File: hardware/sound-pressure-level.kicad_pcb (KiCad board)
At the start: 2 copper layers, 25 x 25 mm, 26 parts, among them P1 CON-SENSOR2, P2 BOOT, U1 XMC1XXX48, U2 DRILL, U3 DRILL, U4 DRILL, U5 DRILL, U6 ICS-43432, X1 16MHz

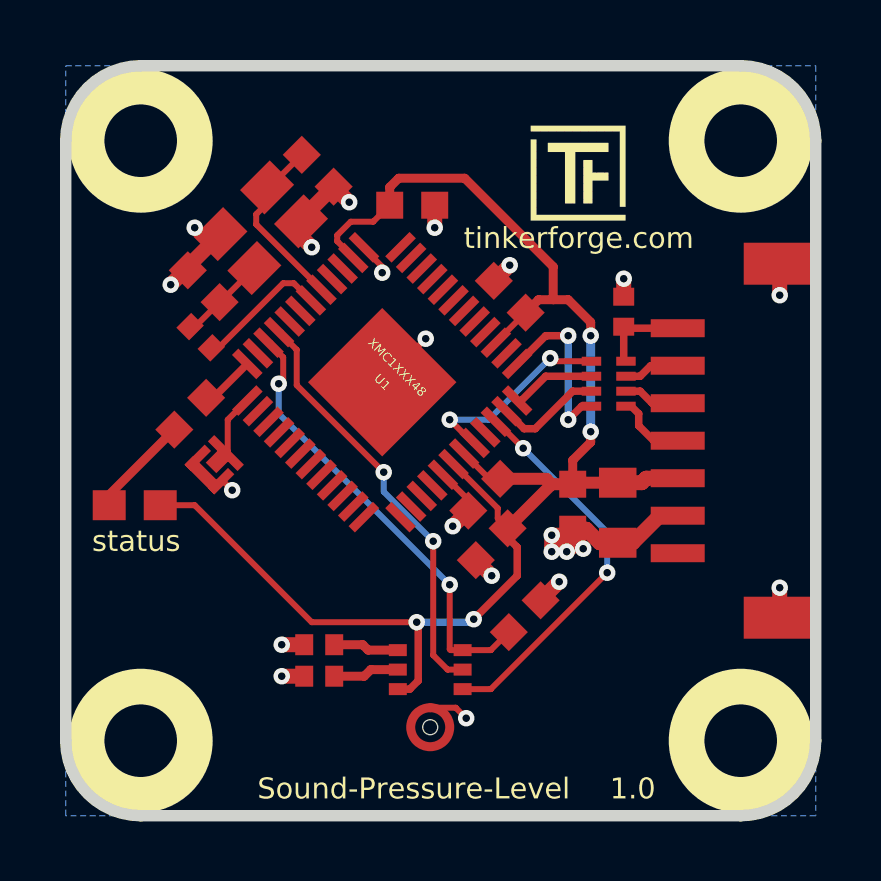
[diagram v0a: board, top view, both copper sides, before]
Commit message: Add capacitor for microphone & logos
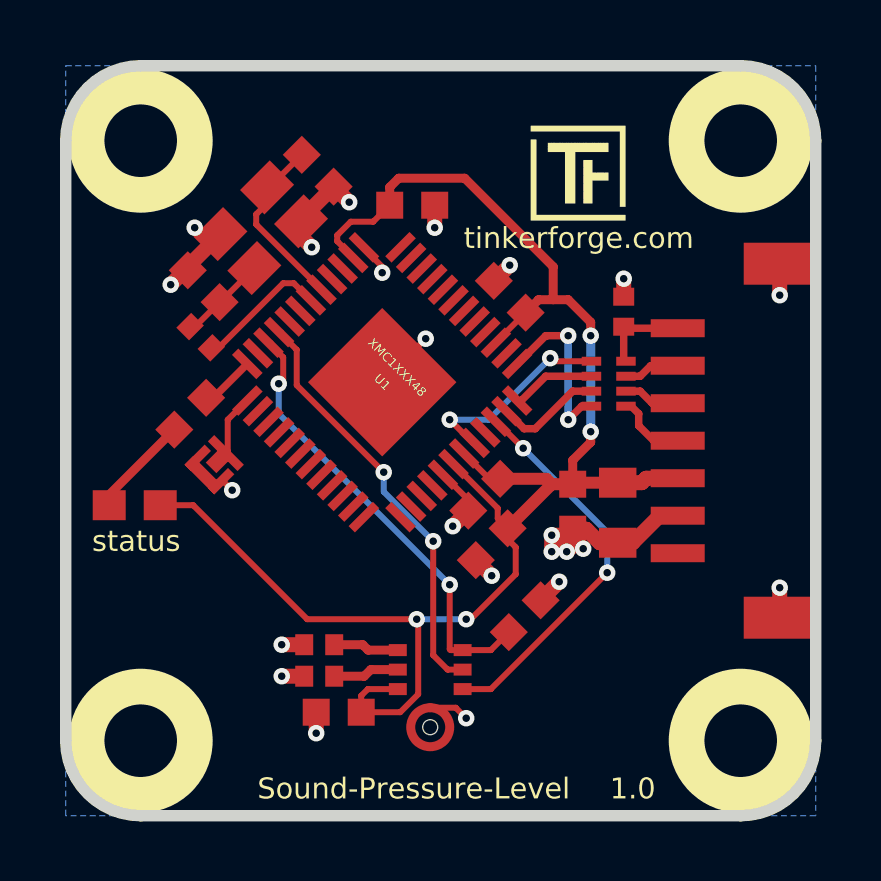
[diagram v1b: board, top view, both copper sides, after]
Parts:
- added C10: 100nF, kicad-libraries:C0603F, F.Cu at (139.2, 150.1)
- added G***: LOGO, kicad-libraries:Logo_CoMCU, B.Cu at (147.1, 132.2)
- added VAL: WEEE_7mm, kicad-libraries:WEEE_7mm, B.Cu at (133.9, 141.0)
- added VAL: CE_5mm, kicad-libraries:CE_5mm, B.Cu at (150.1, 141.0)
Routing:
- net VCC: track 52.6 -> 56.5 mm
- net GND: track 29.8 -> 32.4 mm, vias 22 -> 23

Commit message: add fiducial marks
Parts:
- added Fiducial_Mark: VAL**, kicad-libraries:Fiducial_Mark, F.Cu at (131.6, 135.0)
- added Fiducial_Mark: VAL**, kicad-libraries:Fiducial_Mark, F.Cu at (153.6, 144.5)
- added Fiducial_Mark: VAL**, kicad-libraries:Fiducial_Mark, F.Cu at (134.6, 147.5)
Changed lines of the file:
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@@
-(kicad_pcb (version 4) (host pcbnew 4.0.2+dfsg1-stable)
+(kicad_pcb (version 4) (host pcbnew 4.0.7-e2-6376~58~ubuntu17.04.1)
   (general
     (links 61)
     (no_connects 0)
-    (area 129.909499 128.309499 155.290501 153.690501)
+    (area 129.244999 127.644999 275.49286 158.115)
     (thickness 1.6)
     (drawings 13)
     (tracks 249)
     (zones 0)
-    (modules 30)
+    (modules 33)
     (nets 54)
   )
@@
       (xy 1.301301 2.715081) (xy 1.302426 2.714986)) (layer B.SilkS) (width 0.01))
   )
+  (module kicad-libraries:Fiducial_Mark (layer F.Cu)
+    (at 131.6 135)
+    (attr smd)
+    (fp_text reference Fiducial_Mark (at 0 0) (layer F.SilkS) hide
+      (effects (font (size 0.127 0.127) (thickness 0.03302)))
+    )
+    (fp_text value VAL** (at 0 -0.29972) (layer F.SilkS) hide
+      (effects (font (size 0.127 0.127) (thickness 0.03302)))
+    )
+    (fp_circle (center 0 0) (end 1.15062 0) (layer Dwgs.User) (width 0.01016))
+    (pad 1 smd circle (at 0 0) (size 1.00076 1.00076) (layers F.Cu F.Paste F.Mask)
+      (clearance 0.65024))
+  )
+  (module kicad-libraries:Fiducial_Mark (layer F.Cu)
+    (at 153.6 144.5)
+    (attr smd)
+    (fp_text reference Fiducial_Mark (at 0 0) (layer F.SilkS) hide
+      (effects (font (size 0.127 0.127) (thickness 0.03302)))
+    )
+    (fp_text value VAL** (at 0 -0.29972) (layer F.SilkS) hide
+      (effects (font (size 0.127 0.127) (thickness 0.03302)))
+    )
+    (fp_circle (center 0 0) (end 1.15062 0) (layer Dwgs.User) (width 0.01016))
+    (pad 1 smd circle (at 0 0) (size 1.00076 1.00076) (layers F.Cu F.Paste F.Mask)
+      (clearance 0.65024))
+  )
+  (module kicad-libraries:Fiducial_Mark (layer F.Cu)
+    (at 134.6 147.5)
+    (attr smd)
+    (fp_text reference Fiducial_Mark (at 0 0) (layer F.SilkS) hide
+      (effects (font (size 0.127 0.127) (thickness 0.03302)))
+    )
+    (fp_text value VAL** (at 0 -0.29972) (layer F.SilkS) hide
+      (effects (font (size 0.127 0.127) (thickness 0.03302)))
+    )
+    (fp_circle (center 0 0) (end 1.15062 0) (layer Dwgs.User) (width 0.01016))
+    (pad 1 smd circle (at 0 0) (size 1.00076 1.00076) (layers F.Cu F.Paste F.Mask)
+      (clearance 0.65024))
+  )
   (gr_line (start 152.6 128.5) (end 132.6 128.5) (angle 90) (layer Edge.Cuts) (width 0.381))

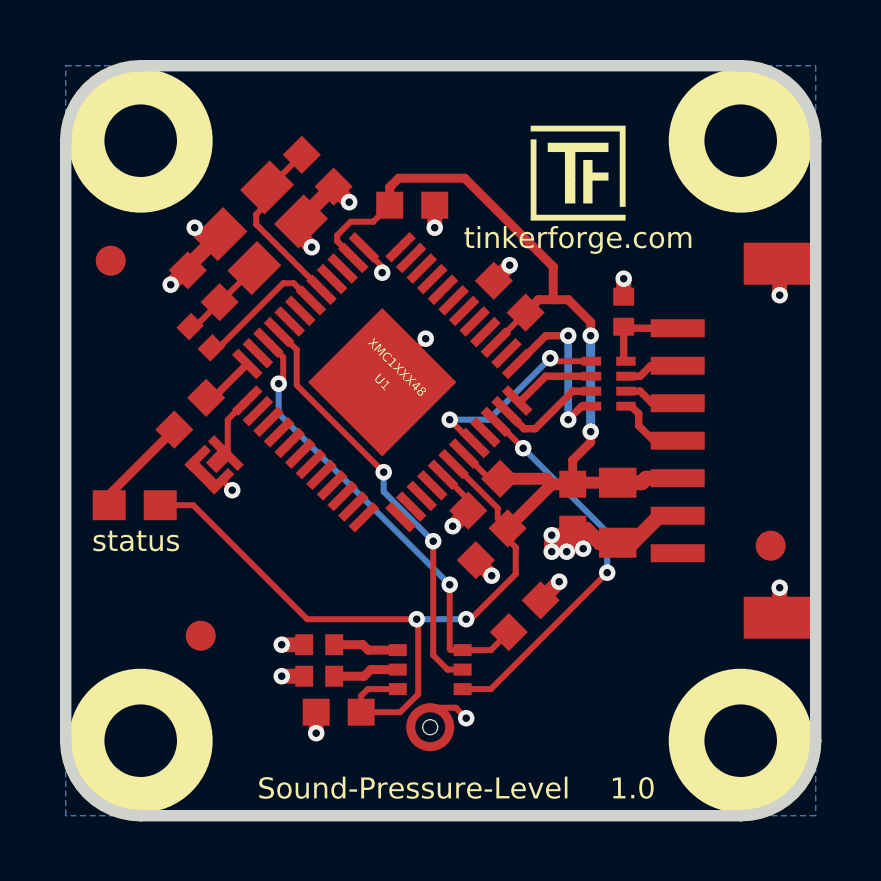
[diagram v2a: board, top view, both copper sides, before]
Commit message: Remove R9
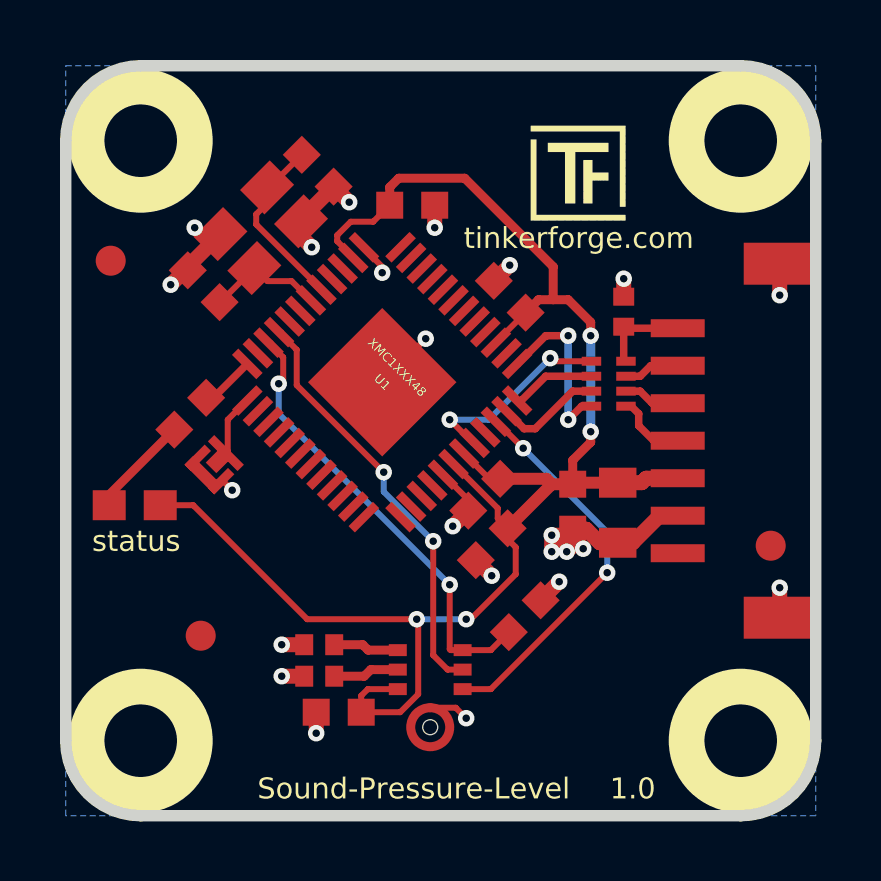
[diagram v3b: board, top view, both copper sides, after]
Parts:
- removed R9: TBD, kicad-libraries:R0402F
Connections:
- U1 pad 42: Net-(R9-Pad1) -> Net-(C9-Pad1)
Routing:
- net Net-(R9-Pad1): track 4.45 -> 0.00 mm
- net Net-(C9-Pad1): track 2.95 -> 3.96 mm

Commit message: Add debug pad
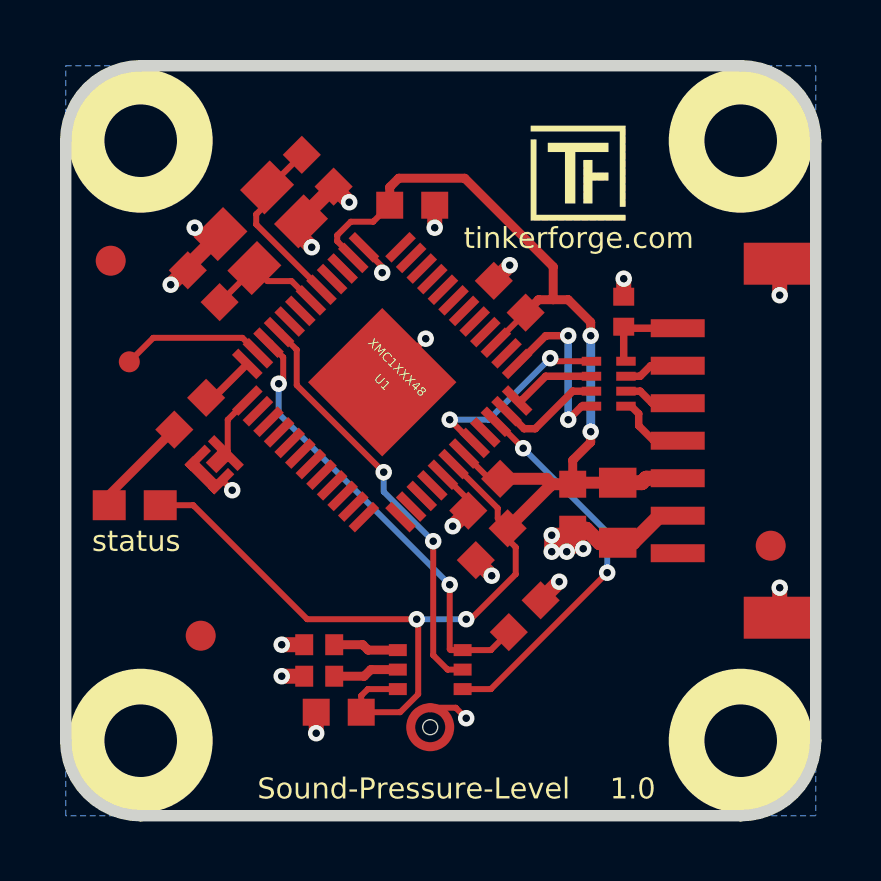
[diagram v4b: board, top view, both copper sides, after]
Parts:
- added P3: DEBUG, kicad-libraries:DEBUG_PAD, F.Cu at (132.2, 138.4)
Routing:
- net Net-(P3-Pad1): track 0.00 -> 4.83 mm
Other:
- board text added: "Copyright Tinkerforge GmbH 2018. This documentation describes Open Hardware and is licensed under the CERN OHL v. 1.1. You may redistribute and modify this documentation under the terms of the CERN OHL v.1.1. (http://ohwr.org/cernohl). This documentation is distributed WITHOUT ANY EXPRESS OR IMPLIED WARRANTY, INCLUDING OF MERCHANTABILITY, SATISFACTORY QUALITY AND FITNESS FOR A PARTICULAR PURPOSE.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"
- board text removed: "Copyright Tinkerforge GmbH 2017. This documentation describes Open Hardware and is licensed under the CERN OHL v. 1.1. You may redistribute and modify this documentation under the terms of the CERN OHL v.1.1. (http://ohwr.org/cernohl). This documentation is distributed WITHOUT ANY EXPRESS OR IMPLIED WARRANTY, INCLUDING OF MERCHANTABILITY, SATISFACTORY QUALITY AND FITNESS FOR A PARTICULAR PURPOSE.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"
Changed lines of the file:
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@@
 (kicad_pcb (version 4) (host pcbnew 4.0.2+dfsg1-stable)
   (general
-    (links 60)
+    (links 61)
     (no_connects 0)
     (area 129.909499 128.309499 155.290501 153.690501)
     (thickness 1.6)
     (drawings 13)
-    (tracks 247)
+    (tracks 251)
     (zones 0)
-    (modules 32)
+    (modules 33)
     (nets 53)
   )
@@
   (title_block
     (title "Sound-Level-Pressure Bricklet")
-    (date 2017-11-30)
+    (date 2018-01-22)
     (rev 1.0)
     (company "Tinkerforge GmbH")
     (comment 1 "Licensed under CERN OHL v.1.1")
-    (comment 2 "Copyright (©) 2017, L.Lauer <lukas@tinkerforge.com>")
+    (comment 2 "Copyright (©) 2018, L.Lauer <lukas@tinkerforge.com>")
   )
   (layers
@@
   (net 48 "Net-(U1-Pad44)")
   (net 49 SCK)
-  (net 50 "Net-(U1-Pad47)")
-  (net 51 "Net-(R3-Pad1)")
-  (net 52 "Net-(R4-Pad1)")
+  (net 50 "Net-(R3-Pad1)")
+  (net 51 "Net-(R4-Pad1)")
+  (net 52 "Net-(P3-Pad1)")
   (net_class Default "This is the default net class."
     (clearance 0.15)
@@
     (add_net "Net-(P1-Pad6)")
     (add_net "Net-(P2-Pad2)")
+    (add_net "Net-(P3-Pad1)")
     (add_net "Net-(R1-Pad1)")
     (add_net "Net-(R3-Pad1)")
@@
     (add_net "Net-(U1-Pad43)")
     (add_net "Net-(U1-Pad44)")
-    (add_net "Net-(U1-Pad47)")
     (add_net "Net-(U1-Pad5)")
     (add_net "Net-(U1-Pad6)")
@@
       (net 17 SD))
     (pad 47 smd rect (at -3.61188 2.2479 45) (size 0.29972 1.14808) (layers F.Cu F.Paste F.Mask)
-      (net 50 "Net-(U1-Pad47)"))
+      (net 52 "Net-(P3-Pad1)"))
     (pad 48 smd rect (at -3.61188 2.74828 45) (size 0.29972 1.14808) (layers F.Cu F.Paste F.Mask)
       (net 16 "Net-(R1-Pad1)"))
@@
       (net 2 VCC))
     (pad 1 smd rect (at -2.57 1.08 270) (size 0.4 0.6) (layers F.Cu F.Paste F.Mask)
-      (net 51 "Net-(R3-Pad1)"))
+      (net 50 "Net-(R3-Pad1)"))
     (pad 2 smd rect (at -1.92 1.08 270) (size 0.4 0.6) (layers F.Cu F.Paste F.Mask)
-      (net 52 "Net-(R4-Pad1)"))
+      (net 51 "Net-(R4-Pad1)"))
   )
   (module kicad-libraries:CRYSTAL_3225 (layer F.Cu)
@@
       (net 1 GND))
     (pad 1 smd rect (at -0.5 0 180) (size 0.6 0.7) (layers F.Cu F.Paste F.Mask)
-      (net 51 "Net-(R3-Pad1)"))
+      (net 50 "Net-(R3-Pad1)"))
     (model Resistors_SMD/R_0402.wrl
       (at (xyz 0 0 0))
@@
       (net 1 GND))
     (pad 1 smd rect (at -0.5 0 180) (size 0.6 0.7) (layers F.Cu F.Paste F.Mask)
-      (net 52 "Net-(R4-Pad1)"))
+      (net 51 "Net-(R4-Pad1)"))
     (model Resistors_SMD/R_0402.wrl
       (at (xyz 0 0 0))
@@
       (clearance 0.65024))
   )
+  (module kicad-libraries:DEBUG_PAD (layer F.Cu)
+    (at 132.22 138.37)
+    (fp_text reference P3 (at 0 0.175) (layer F.Fab)
+      (effects (font (size 0.15 0.15) (thickness 0.0375)))
+    )
+    (fp_text value DEBUG (at 0 -0.15) (layer F.Fab)
+      (effects (font (size 0.15 0.15) (thickness 0.0375)))
+    )
+    (pad 1 smd circle (at 0 0) (size 0.7 0.7) (layers F.Cu F.Paste F.Mask)
+      (net 52 "Net-(P3-Pad1)"))
+  )
   (gr_line (start 152.6 128.5) (end 132.6 128.5) (angle 90) (layer Edge.Cuts) (width 0.381))
   (gr_line (start 132.6 153.5) (end 152.6 153.5) (angle 90) (layer Edge.Cuts) (width 0.381))
-  (gr_text "Copyright Tinkerforge GmbH 2017.\nThis documentation describes Open Hardware and is licensed under the\nCERN OHL v. 1.1.\nYou may redistribute and modify this documentation under the terms of the\nCERN OHL v.1.1. (http://ohwr.org/cernohl). This documentation is distributed\nWITHOUT ANY EXPRESS OR IMPLIED WARRANTY, INCLUDING OF\nMERCHANTABILITY, SATISFACTORY QUALITY AND FITNESS FOR A\nPARTICULAR PURPOSE. Please see the CERN OHL v.1.1 for applicable\nconditions" (at 251.55 152) (layer Cmts.User)
+  (gr_text "Copyright Tinkerforge GmbH 2018.\nThis documentation describes Open Hardware and is licensed under the\nCERN OHL v. 1.1.\nYou may redistribute and modify this documentation under the terms of the\nCERN OHL v.1.1. (http://ohwr.org/cernohl). This documentation is distributed\nWITHOUT ANY EXPRESS OR IMPLIED WARRANTY, INCLUDING OF\nMERCHANTABILITY, SATISFACTORY QUALITY AND FITNESS FOR A\nPARTICULAR PURPOSE. Please see the CERN OHL v.1.1 for applicable\nconditions" (at 37.91 189.93) (layer Cmts.User)
     (effects (font (size 0.8 0.8) (thickness 0.15)))
   )
@@
   (segment (start 136.45 133.45) (end 136.45 133.79033) (width 0.2) (layer F.Cu) (net 8))
   (segment (start 136.45 133.79033) (end 138.62585 135.96618) (width 0.2) (layer F.Cu) (net 8))
-  (segment (start 138.272028 136.320002) (end 138.270002 136.320002) (width 0.2) (layer F.Cu) (net 9) (status C00000))
-  (segment (start 138.270002 136.320002) (end 137.63 135.68) (width 0.2) (layer F.Cu) (net 9) (status 400000))
+  (segment (start 138.272028 136.320002) (end 138.270002 136.320002) (width 0.2) (layer F.Cu) (net 9))
+  (segment (start 138.270002 136.320002) (end 137.63 135.68) (width 0.2) (layer F.Cu) (net 9))
   (segment (start 137.63 135.68) (end 136.82462 135.68) (width 0.2) (layer F.Cu) (net 9))
-  (segment (start 136.82462 135.68) (end 136.388066 135.243446) (width 0.2) (layer F.Cu) (net 9) (status 800000))
+  (segment (start 136.82462 135.68) (end 136.388066 135.243446) (width 0.2) (layer F.Cu) (net 9))
   (segment (start 135.23033 136.38033) (end 135.251182 136.38033) (width 0.2) (layer F.Cu) (net 9))
   (segment (start 135.251182 136.38033) (end 136.388066 135.243446) (width 0.2) (layer F.Cu) (net 9))
@@
   (segment (start 137.279672 137.379672) (end 137.212358 137.379672) (width 0.2) (layer F.Cu) (net 49))
   (segment (start 137.212358 137.412358) (end 137.212358 137.379672) (width 0.2) (layer F.Cu) (net 49))
-  (segment (start 139.05 147.8) (end 140 147.8) (width 0.3) (layer F.Cu) (net 51))
-  (segment (start 140.18 147.98) (end 141.17 147.98) (width 0.3) (layer F.Cu) (net 51))
-  (segment (start 140 147.8) (end 140.18 147.98) (width 0.3) (layer F.Cu) (net 51))
-  (segment (start 141.17 148.63) (end 140.27 148.63) (width 0.3) (layer F.Cu) (net 52))
-  (segment (start 140.05 148.85) (end 139.05 148.85) (width 0.3) (layer F.Cu) (net 52))
-  (segment (start 140.27 148.63) (end 140.05 148.85) (width 0.3) (layer F.Cu) (net 52))
+  (segment (start 139.05 147.8) (end 140 147.8) (width 0.3) (layer F.Cu) (net 50))
+  (segment (start 140.18 147.98) (end 141.17 147.98) (width 0.3) (layer F.Cu) (net 50))
+  (segment (start 140 147.8) (end 140.18 147.98) (width 0.3) (layer F.Cu) (net 50))
+  (segment (start 141.17 148.63) (end 140.27 148.63) (width 0.3) (layer F.Cu) (net 51))
+  (segment (start 140.05 148.85) (end 139.05 148.85) (width 0.3) (layer F.Cu) (net 51))
+  (segment (start 140.27 148.63) (end 140.05 148.85) (width 0.3) (layer F.Cu) (net 51))
+  (segment (start 136.50651 138.08552) (end 136.50552 138.08552) (width 0.2) (layer F.Cu) (net 52))
+  (segment (start 136.50552 138.08552) (end 135.99 137.57) (width 0.2) (layer F.Cu) (net 52))
+  (segment (start 135.99 137.57) (end 133.02 137.57) (width 0.2) (layer F.Cu) (net 52))
+  (segment (start 133.02 137.57) (end 132.22 138.37) (width 0.2) (layer F.Cu) (net 52))
   (zone (net 1) (net_name GND) (layer B.Cu) (hatch edge 0.508)
     (connect_pads yes (clearance 0.2))
